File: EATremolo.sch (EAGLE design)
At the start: 34 parts, among them Q1 2N5457, Q2 2N3904, Q3 2N5457, Q4 2N5088

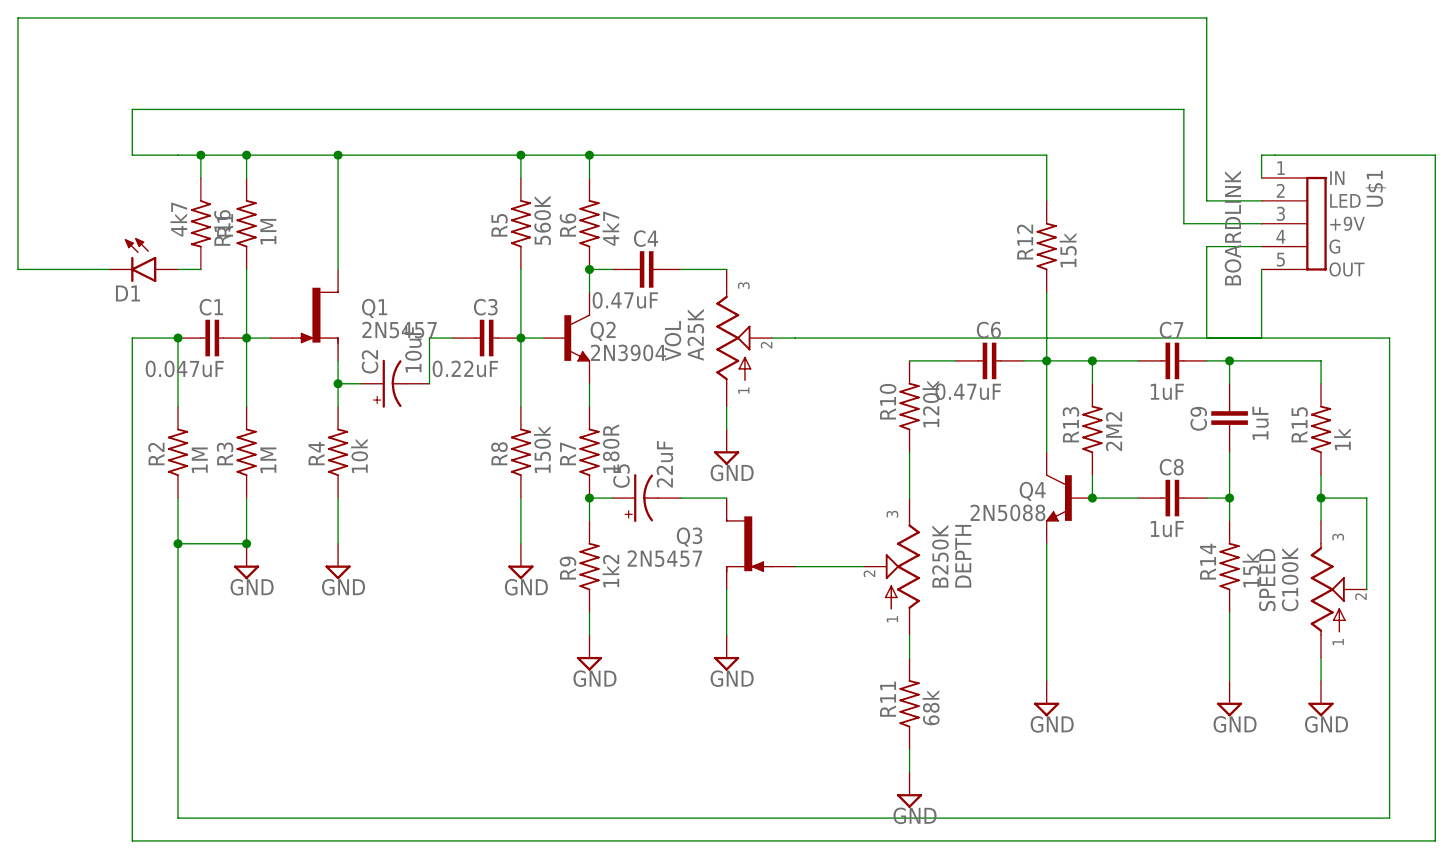
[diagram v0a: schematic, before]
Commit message: Fixed issue where speed pot was wired (and laid out) backwards
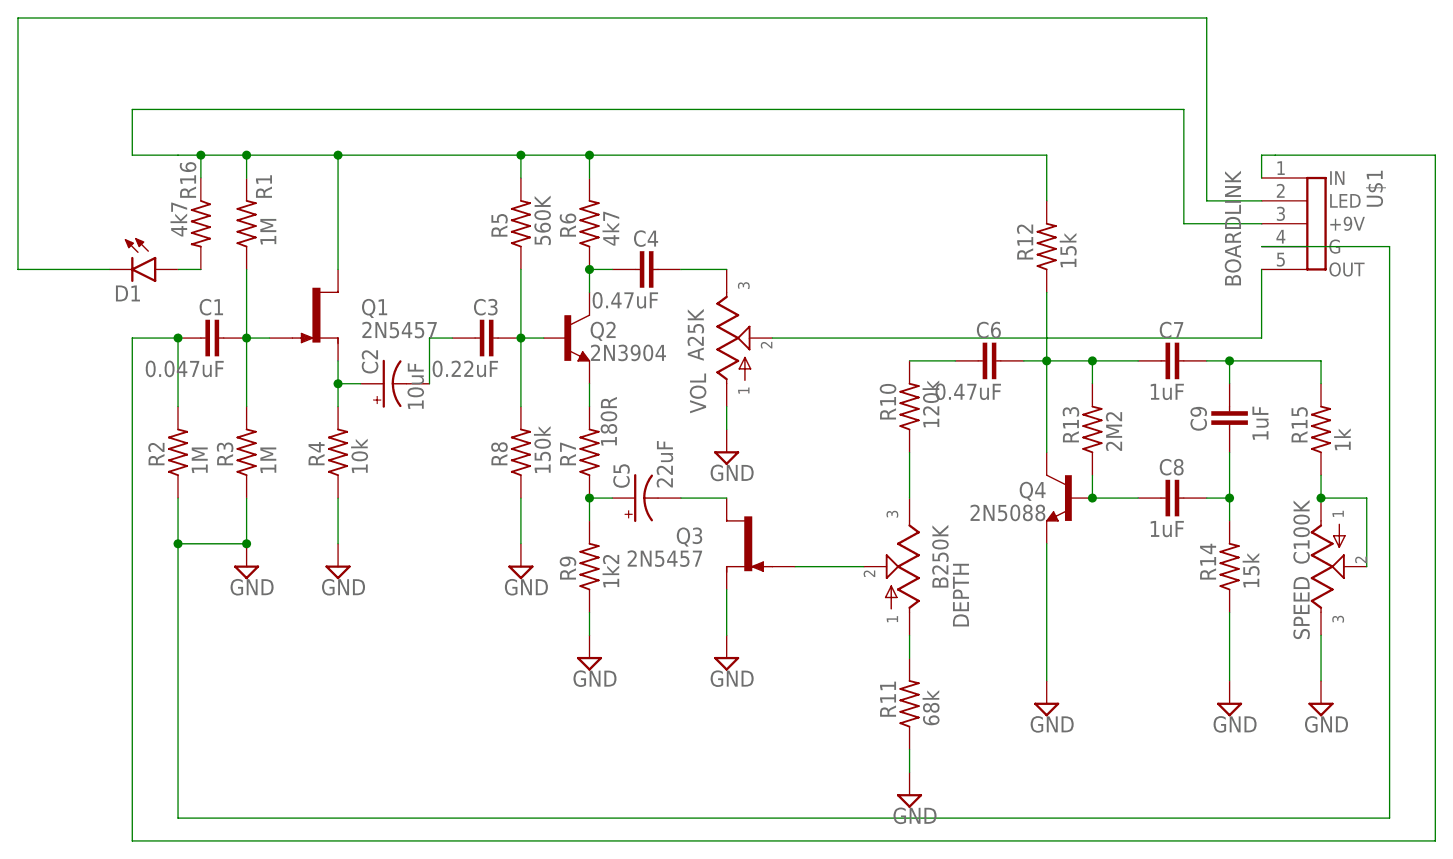
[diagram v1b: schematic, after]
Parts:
- C7, C8, C9: device mb_caps-box:072X0352 -> mb_caps-box:072X0452
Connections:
- net GND: now also SPEED.3; no longer SPEED.1
- net N$19: now also SPEED.1; no longer SPEED.3
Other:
- moved on the sheet: SPEED

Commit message: Updated MMBF5457 to right footprint
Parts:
- added U$2, U$3: MMBF5457, xc_library:MMBF5457
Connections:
- net GND: now also U$3.D
- net N$11: now also U$3.G
- net N$2: now also U$2.G
- net N$22: now also U$2.D
- net N$4: now also U$2.S
- net N$9: now also U$3.S

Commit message: Fixed issue with SMD 5457
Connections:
- net GND: now also U$3.S; no longer U$3.D
- net N$9: now also U$3.D; no longer U$3.S
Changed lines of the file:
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@@
 <pinref part="GND3" gate="GND" pin="GND"/>
 <wire x1="66.04" y1="27.94" x2="66.04" y2="22.86" width="0.1524" layer="91"/>
-<pinref part="U$3" gate="G$1" pin="D"/>
-<wire x1="73.66" y1="35.56" x2="73.66" y2="27.94" width="0.1524" layer="91"/>
-<wire x1="73.66" y1="27.94" x2="66.04" y2="27.94" width="0.1524" layer="91"/>
+<wire x1="66.04" y1="27.94" x2="72.136" y2="27.94" width="0.1524" layer="91"/>
+<wire x1="72.136" y1="27.94" x2="72.136" y2="27.686" width="0.1524" layer="91"/>
 <junction x="66.04" y="27.94"/>
+<wire x1="72.136" y1="27.94" x2="72.136" y2="45.72" width="0.1524" layer="91"/>
+<pinref part="U$3" gate="G$1" pin="S"/>
+<wire x1="72.136" y1="45.72" x2="73.66" y2="45.72" width="0.1524" layer="91"/>
 </segment>
 <segment>
@@
 <pinref part="Q3" gate="G$1" pin="D"/>
 <wire x1="60.96" y1="38.1" x2="66.04" y2="38.1" width="0.1524" layer="91"/>
-<pinref part="U$3" gate="G$1" pin="S"/>
-<wire x1="73.66" y1="45.72" x2="68.58" y2="45.72" width="0.1524" layer="91"/>
-<wire x1="68.58" y1="45.72" x2="68.58" y2="38.1" width="0.1524" layer="91"/>
-<wire x1="68.58" y1="38.1" x2="66.04" y2="38.1" width="0.1524" layer="91"/>
+<pinref part="U$3" gate="G$1" pin="D"/>
+<wire x1="73.66" y1="35.56" x2="71.12" y2="35.56" width="0.1524" layer="91"/>
+<wire x1="71.12" y1="35.56" x2="71.12" y2="38.1" width="0.1524" layer="91"/>
+<wire x1="71.12" y1="38.1" x2="66.04" y2="38.1" width="0.1524" layer="91"/>
 <junction x="66.04" y="38.1"/>
 </segment>

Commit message: Version 1.0 of Tremolo Thing
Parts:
- C1: value 0.047uF -> 47nF
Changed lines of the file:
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@@
 <?xml version="1.0" encoding="utf-8"?>
 <!DOCTYPE eagle SYSTEM "eagle.dtd">
-<eagle version="9.2.2">
+<eagle version="9.5.2">
 <drawing>
 <settings>
@@
 <part name="R14" library="mb_resistors" deviceset="6MM" device=".3" value="15k"/>
 <part name="R15" library="mb_resistors" deviceset="6MM" device=".3" value="1k"/>
-<part name="C1" library="mb_caps-box" deviceset="072X025" device="2" value="0.047uF"/>
+<part name="C1" library="mb_caps-box" deviceset="072X025" device="2" value="47nF"/>
 <part name="C2" library="mb_caps-electro" deviceset="050" device="1" value="10uF"/>
 <part name="C3" library="mb_caps-box" deviceset="072X035" device="2" value="0.22uF"/>
